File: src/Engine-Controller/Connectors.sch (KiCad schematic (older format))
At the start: 3 parts

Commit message: Annotated Schematic
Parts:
- removed None?: +VIN, symbol Engine-Controller:+VIN
- gave numbers to parts that had none: 2
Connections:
- net labels added: +VIN
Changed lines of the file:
@@
 $EndDescr
 $Comp
-L Engine-Controller:0901471110 J?
+L Engine-Controller:0901471110 J5
 U 1 1 60E3A3F9
 P 9150 1950
-F 0 "J?" H 9678 1553 60  0000 L CNN
+F 0 "J5" H 9678 1553 60  0000 L CNN
 F 1 "0901471110" H 9678 1447 60  0000 L CNN
 F 2 "66953-005LF_AMP" H 9300 750 60  0001 C CNN
@@
 	9050 4900 8800 4900
 $Comp
-L power:Earth #PWR?
+L power:Earth #PWR0112
 U 1 1 60DBDE57
 P 8800 5600
-F 0 "#PWR?" H 8800 5350 50  0001 C CNN
+F 0 "#PWR0112" H 8800 5350 50  0001 C CNN
 F 1 "Earth" H 8800 5450 50  0001 C CNN
 F 2 "" H 8800 5600 50  0001 C CNN
@@
 	9050 4400 8700 4400
 $Comp
-L Engine-Controller:+VIN None?
+L Engine-Controller:+VIN #None0101
 U 1 1 60E48282
 P 8700 4100
-F 0 "None?" H 8800 4100 50  0001 L CNN
+F 0 "#None0101" H 8800 4100 50  0001 L CNN
 F 1 "+VIN" H 8600 4200 50  0000 L CNN
 F 2 "" H 8700 4100 50  0001 C CNN
@@
 $EndComp
 $Comp
-L Engine-Controller:66953-005LF J?
+L Engine-Controller:66953-005LF J4
 U 1 1 60E41099
 P 9050 4400
-F 0 "J?" H 9578 4003 60  0000 L CNN
+F 0 "J4" H 9578 4003 60  0000 L CNN
 F 1 "66953-005LF" H 9578 3897 60  0000 L CNN
 F 2 "66953-005LF_AMP" H 9200 3200 60  0001 C CNN

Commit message: Associated Schematic Symbols with footprints
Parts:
- J5: footprint 66953-005LF_AMP -> Engine-Controller:0901471110
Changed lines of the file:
@@
 F 0 "J5" H 9678 1553 60  0000 L CNN
 F 1 "0901471110" H 9678 1447 60  0000 L CNN
-F 2 "66953-005LF_AMP" H 9300 750 60  0001 C CNN
+F 2 "Engine-Controller:0901471110" H 9300 750 60  0001 C CNN
 F 3 "" H 9150 1950 60  0000 C CNN
 	1    9150 1950

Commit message: Resolved all ERC issues
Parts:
- J4: footprint 66953-005LF_AMP -> Engine-Controller:66953-005LF
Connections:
- net labels removed: +VIN
- wire segments 23 -> 21
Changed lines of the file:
@@
 Comment4 ""
 $EndDescr
-$Comp
-L Engine-Controller:0901471110 J5
-U 1 1 60E3A3F9
-P 9150 1950
-F 0 "J5" H 9678 1553 60  0000 L CNN
-F 1 "0901471110" H 9678 1447 60  0000 L CNN
-F 2 "Engine-Controller:0901471110" H 9300 750 60  0001 C CNN
-F 3 "" H 9150 1950 60  0000 C CNN
-	1    9150 1950
-	1    0    0    -1
-$EndComp
 Text Notes 8300 1600 0    50   ~ 0
 IO Connector\n
@@
 	1    0    0    -1
 $EndComp
-Connection ~ 8700 4400
-Wire Wire Line
-	8550 4400 8700 4400
 Text GLabel 8550 4400 0    50   Input ~ 0
 VIN
-Wire Wire Line
-	8700 4400 8700 4250
-Wire Wire Line
-	9050 4400 8700 4400
-$Comp
-L Engine-Controller:+VIN #None0101
-U 1 1 60E48282
-P 8700 4100
-F 0 "#None0101" H 8800 4100 50  0001 L CNN
-F 1 "+VIN" H 8600 4200 50  0000 L CNN
-F 2 "" H 8700 4100 50  0001 C CNN
-F 3 "" H 8700 4100 50  0001 C CNN
-	1    8700 4100
-	1    0    0    -1
-$EndComp
-$Comp
-L Engine-Controller:66953-005LF J4
-U 1 1 60E41099
-P 9050 4400
-F 0 "J4" H 9578 4003 60  0000 L CNN
-F 1 "66953-005LF" H 9578 3897 60  0000 L CNN
-F 2 "66953-005LF_AMP" H 9200 3200 60  0001 C CNN
-F 3 "" H 9050 4400 60  0000 C CNN
-	1    9050 4400
-	1    0    0    -1
-$EndComp
 Wire Notes Line
 	10400 3900 10400 5800
@@
 Text GLabel 8100 2850 0    50   Input ~ 0
 IO10
-Wire Wire Line
-	9150 1950 8050 1950
-Wire Wire Line
-	9150 2050 8050 2050
-Wire Wire Line
-	9150 2150 8050 2150
-Wire Wire Line
-	9150 2250 8050 2250
-Wire Wire Line
-	9150 2350 8050 2350
-Wire Wire Line
-	9150 2450 8050 2450
-Wire Wire Line
-	9150 2550 8050 2550
-Wire Wire Line
-	9150 2650 8050 2650
-Wire Wire Line
-	9150 2750 8050 2750
-Wire Wire Line
-	9150 2850 8100 2850
 Wire Notes Line
 	7200 3200 7200 1700
@@
 Wire Notes Line
 	10450 3200 7200 3200
+$Comp
+L Engine-Controller:0901471110 J5
+U 1 1 6119F1F0
+P 9300 1950
+F 0 "J5" H 9828 1553 60  0000 L CNN
+F 1 "0901471110" H 9828 1447 60  0000 L CNN
+F 2 "Engine-Controller:0901471110" H 9450 750 60  0001 C CNN
+F 3 "" H 9300 1950 60  0000 C CNN
+	1    9300 1950
+	1    0    0    -1
+$EndComp
+Wire Wire Line
+	9300 1950 8050 1950
+Wire Wire Line
+	9300 2050 8050 2050
+Wire Wire Line
+	9300 2150 8050 2150
+Wire Wire Line
+	9300 2250 8050 2250
+Wire Wire Line
+	9300 2350 8050 2350
+Wire Wire Line
+	9300 2450 8050 2450
+Wire Wire Line
+	9300 2550 8050 2550
+Wire Wire Line
+	9300 2650 8050 2650
+Wire Wire Line
+	9300 2750 8050 2750
+Wire Wire Line
+	9300 2850 8100 2850
+$Comp
+L Engine-Controller:66953-005LF J4
+U 1 1 612955EA
+P 9050 4400
+F 0 "J4" H 9578 4003 60  0000 L CNN
+F 1 "66953-005LF" H 9578 3897 60  0000 L CNN
+F 2 "Engine-Controller:66953-005LF" H 9200 3200 60  0001 C CNN
+F 3 "" H 9050 4400 60  0000 C CNN
+	1    9050 4400
+	1    0    0    -1
+$EndComp
+Wire Wire Line
+	8550 4400 9050 4400
 $EndSCHEMATC

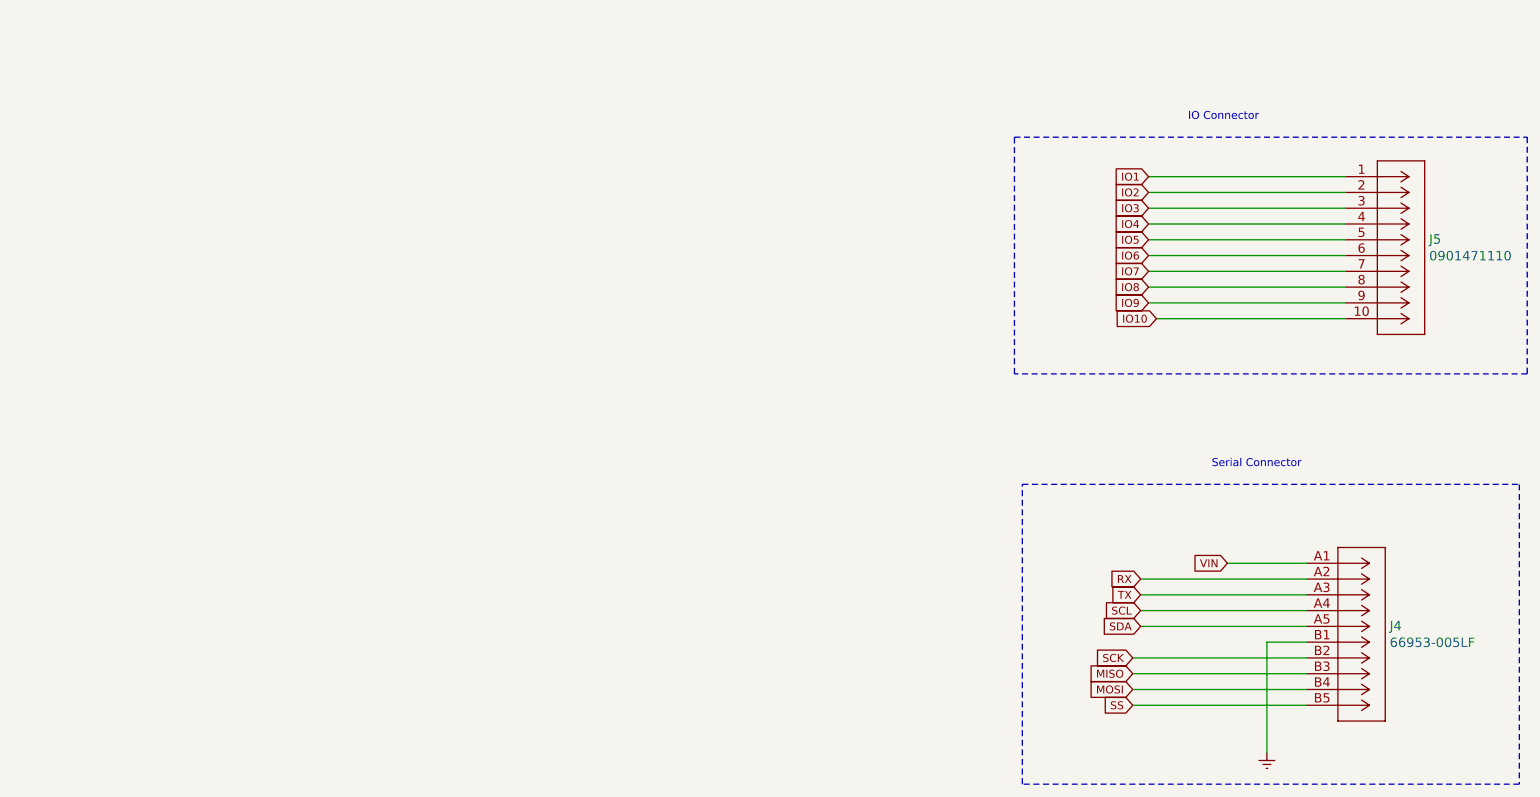
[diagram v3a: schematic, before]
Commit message: Added buffer to some IOs
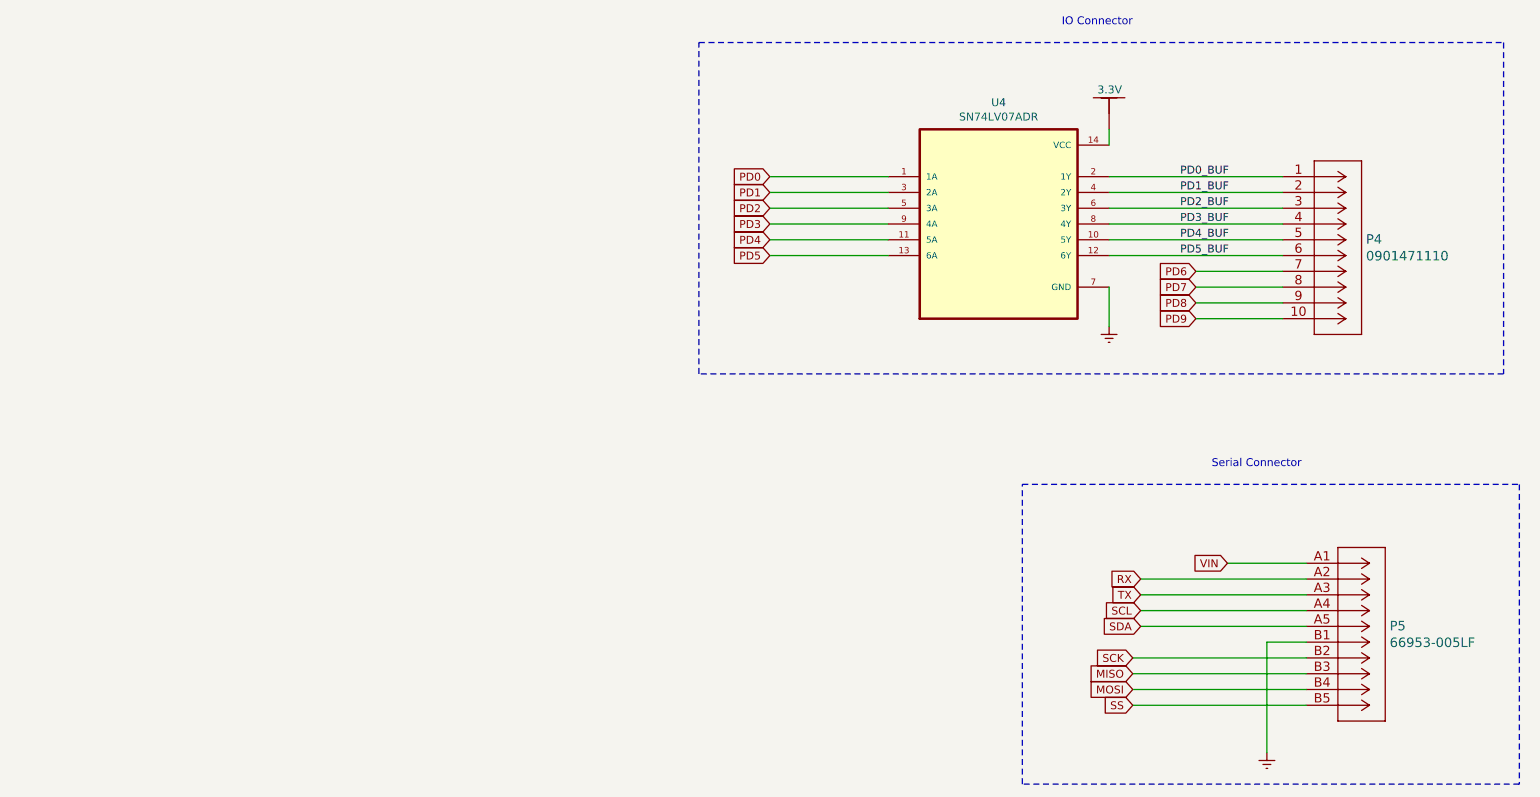
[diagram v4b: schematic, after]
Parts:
- removed J4: 66953-005LF, Engine-Controller:66953-005LF, symbol Engine-Controller:66953-005LF
- removed J5: 0901471110, Engine-Controller:0901471110, symbol Engine-Controller:0901471110
- added None02: 3.3V, symbol Engine-Controller:3.3V
- added P4: 0901471110, 66953-005LF_AMP, symbol Engine-Controller:0901471110
- added P5: 66953-005LF, 66953-005LF_AMP, symbol Engine-Controller:66953-005LF
- added U4: SN74LV07ADR, SOIC127P600X175-14N, symbol Engine-Controller:SN74LV07ADR
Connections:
- net Earth: now also P5.B1, U4.7 (GND)
- net MISO: now also P5.B3
- net MOSI: now also P5.B4
- net RX: now also P5.A2
- net SCK: now also P5.B2
- net SCL: now also P5.A4
- net SDA: now also P5.A5
- net SS: now also P5.B5
- net TX: now also P5.A3
- net VIN: now also P5.A1
- new net: None02.~, U4.14 (VCC)
- new net PD0: U4.1 (1A)
- new net PD0_BUF: P4.1, U4.2 (1Y)
- new net PD1: U4.3 (2A)
- new net PD1_BUF: P4.2, U4.4 (2Y)
- new net PD2: U4.5 (3A)
- new net PD2_BUF: P4.3, U4.6 (3Y)
- new net PD3: U4.9 (4A)
- new net PD3_BUF: P4.4, U4.8 (4Y)
- new net PD4: U4.11 (5A)
- new net PD4_BUF: P4.5, U4.10 (5Y)
- new net PD5: U4.13 (6A)
- new net PD5_BUF: P4.6, U4.12 (6Y)
- new net PD6: P4.7
- new net PD7: P4.8
- new net PD8: P4.9
- new net PD9: P4.10
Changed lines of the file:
@@
 Comment4 ""
 $EndDescr
-Text Notes 8300 1600 0    50   ~ 0
+Text Notes 7500 1000 0    50   ~ 0
 IO Connector\n
 Text Notes 8450 3800 0    50   ~ 0
@@
 Wire Notes Line
 	7250 3900 10400 3900
-Text GLabel 8050 1950 0    50   Input ~ 0
-IO1
-Text GLabel 8050 2050 0    50   Input ~ 0
-IO2
-Text GLabel 8050 2150 0    50   Input ~ 0
-IO3
-Text GLabel 8050 2250 0    50   Input ~ 0
-IO4
-Text GLabel 8050 2350 0    50   Input ~ 0
-IO5
-Text GLabel 8050 2450 0    50   Input ~ 0
-IO6
-Text GLabel 8050 2550 0    50   Input ~ 0
-IO7
-Text GLabel 8050 2650 0    50   Input ~ 0
-IO8
-Text GLabel 8050 2750 0    50   Input ~ 0
-IO9
-Text GLabel 8100 2850 0    50   Input ~ 0
-IO10
-Wire Notes Line
-	7200 3200 7200 1700
-Wire Notes Line
-	7200 1700 10450 1700
-Wire Notes Line
-	10450 1700 10450 3200
-Wire Notes Line
-	10450 3200 7200 3200
+Text GLabel 5650 1950 0    50   Input ~ 0
+PD0
+Text GLabel 5650 2050 0    50   Input ~ 0
+PD1
+Text GLabel 5650 2150 0    50   Input ~ 0
+PD2
+Text GLabel 5650 2250 0    50   Input ~ 0
+PD3
+Text GLabel 5650 2350 0    50   Input ~ 0
+PD4
+Text GLabel 5650 2450 0    50   Input ~ 0
+PD5
+Text GLabel 8350 2550 0    50   Input ~ 0
+PD6
+Text GLabel 8350 2650 0    50   Input ~ 0
+PD7
+Text GLabel 8350 2750 0    50   Input ~ 0
+PD8
+Text GLabel 8350 2850 0    50   Input ~ 0
+PD9
+Wire Wire Line
+	8550 4400 9050 4400
 $Comp
-L Engine-Controller:0901471110 J5
-U 1 1 6119F1F0
-P 9300 1950
-F 0 "J5" H 9828 1553 60  0000 L CNN
-F 1 "0901471110" H 9828 1447 60  0000 L CNN
-F 2 "Engine-Controller:0901471110" H 9450 750 60  0001 C CNN
-F 3 "" H 9300 1950 60  0000 C CNN
-	1    9300 1950
+L Engine-Controller:0901471110 P4
+U 1 1 61252CB3
+P 8900 1950
+F 0 "P4" H 9428 1553 60  0000 L CNN
+F 1 "0901471110" H 9428 1447 60  0000 L CNN
+F 2 "66953-005LF_AMP" H 9050 750 60  0001 C CNN
+F 3 "" H 8900 1950 60  0001 C CNN
+	1    8900 1950
 	1    0    0    -1
 $EndComp
-Wire Wire Line
-	9300 1950 8050 1950
-Wire Wire Line
-	9300 2050 8050 2050
-Wire Wire Line
-	9300 2150 8050 2150
-Wire Wire Line
-	9300 2250 8050 2250
-Wire Wire Line
-	9300 2350 8050 2350
-Wire Wire Line
-	9300 2450 8050 2450
-Wire Wire Line
-	9300 2550 8050 2550
-Wire Wire Line
-	9300 2650 8050 2650
-Wire Wire Line
-	9300 2750 8050 2750
-Wire Wire Line
-	9300 2850 8100 2850
 $Comp
-L Engine-Controller:66953-005LF J4
-U 1 1 612955EA
+L Engine-Controller:66953-005LF P5
+U 1 1 61255D75
 P 9050 4400
-F 0 "J4" H 9578 4003 60  0000 L CNN
+F 0 "P5" H 9578 4003 60  0000 L CNN
 F 1 "66953-005LF" H 9578 3897 60  0000 L CNN
-F 2 "Engine-Controller:66953-005LF" H 9200 3200 60  0001 C CNN
-F 3 "" H 9050 4400 60  0000 C CNN
+F 2 "66953-005LF_AMP" H 9200 3200 60  0001 C CNN
+F 3 "" H 9050 4400 60  0001 C CNN
 	1    9050 4400
 	1    0    0    -1
 $EndComp
 Wire Wire Line
-	8550 4400 9050 4400
+	5650 1950 6400 1950
+Wire Wire Line
+	5650 2050 6400 2050
+Wire Wire Line
+	5650 2150 6400 2150
+Wire Wire Line
+	5650 2250 6400 2250
+Wire Wire Line
+	5650 2350 6400 2350
+Wire Wire Line
+	5650 2450 6400 2450
+Wire Wire Line
+	7800 1950 8900 1950
+Wire Wire Line
+	7800 2050 8900 2050
+Wire Wire Line
+	7800 2150 8900 2150
+Wire Wire Line
+	7800 2250 8900 2250
+Wire Wire Line
+	7800 2350 8900 2350
+Wire Wire Line
+	7800 2450 8900 2450
+$Comp
+L power:Earth #PWR02
+U 1 1 6138D033
+P 7800 2900
+F 0 "#PWR02" H 7800 2650 50  0001 C CNN
+F 1 "Earth" H 7800 2750 50  0001 C CNN
+F 2 "" H 7800 2900 50  0001 C CNN
+F 3 "~" H 7800 2900 50  0001 C CNN
+	1    7800 2900
+	1    0    0    -1
+$EndComp
+Wire Wire Line
+	7800 2650 7800 2900
+$Comp
+L Engine-Controller:3.3V None02
+U 1 1 61392439
+P 7800 1500
+F 0 "None02" H 7928 1489 50  0001 L CNN
+F 1 "3.3V" H 7726 1601 50  0000 L CNN
+F 2 "" H 7800 1500 50  0001 C CNN
+F 3 "" H 7800 1500 50  0001 C CNN
+	1    7800 1500
+	1    0    0    -1
+$EndComp
+$Comp
+L Engine-Controller:SN74LV07ADR U4
+U 1 1 6134C986
+P 7100 2250
+F 0 "U4" H 7100 3020 50  0000 C CNN
+F 1 "SN74LV07ADR" H 7100 2929 50  0000 C CNN
+F 2 "SOIC127P600X175-14N" H 6650 1350 50  0001 L BNN
+F 3 "" H 7100 2250 50  0001 L BNN
+	1    7100 2250
+	1    0    0    -1
+$EndComp
+Wire Wire Line
+	7800 1750 7800 1650
+Wire Notes Line
+	5200 1100 10300 1100
+Wire Notes Line
+	10300 1100 10300 3200
+Wire Notes Line
+	10300 3200 5200 3200
+Wire Notes Line
+	5200 3200 5200 1100
+Text Label 8250 1950 0    50   ~ 0
+PD0_BUF
+Text Label 8250 2050 0    50   ~ 0
+PD1_BUF
+Text Label 8250 2250 0    50   ~ 0
+PD3_BUF
+Text Label 8250 2350 0    50   ~ 0
+PD4_BUF
+Text Label 8250 2150 0    50   ~ 0
+PD2_BUF
+Text Label 8250 2450 0    50   ~ 0
+PD5_BUF
+Wire Wire Line
+	8350 2550 8900 2550
+Wire Wire Line
+	8350 2650 8900 2650
+Wire Wire Line
+	8350 2750 8900 2750
+Wire Wire Line
+	8350 2850 8900 2850
 $EndSCHEMATC

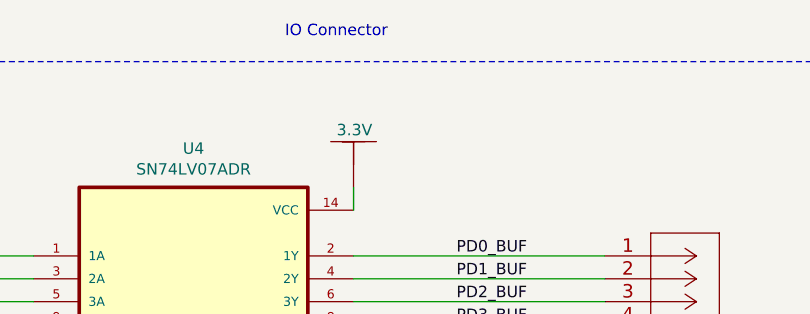
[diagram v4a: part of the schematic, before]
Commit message: Added NO Jumper to NRST button
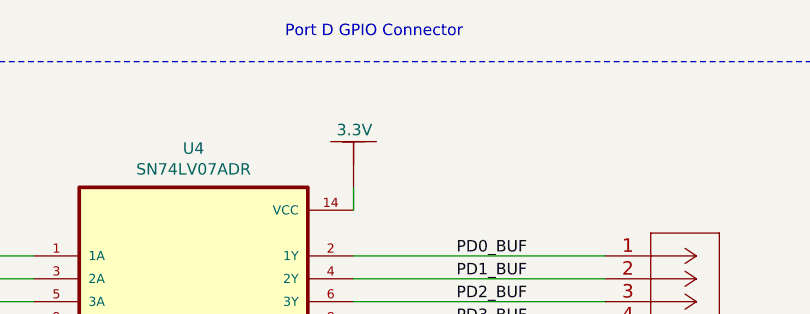
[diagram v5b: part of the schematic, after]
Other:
- note added: "Port D GPIO Connector\n"
- note removed: "IO Connector\n"
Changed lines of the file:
@@
 $EndDescr
 Text Notes 7500 1000 0    50   ~ 0
-IO Connector\n
+Port D GPIO Connector\n
 Text Notes 8450 3800 0    50   ~ 0
 Serial Connector

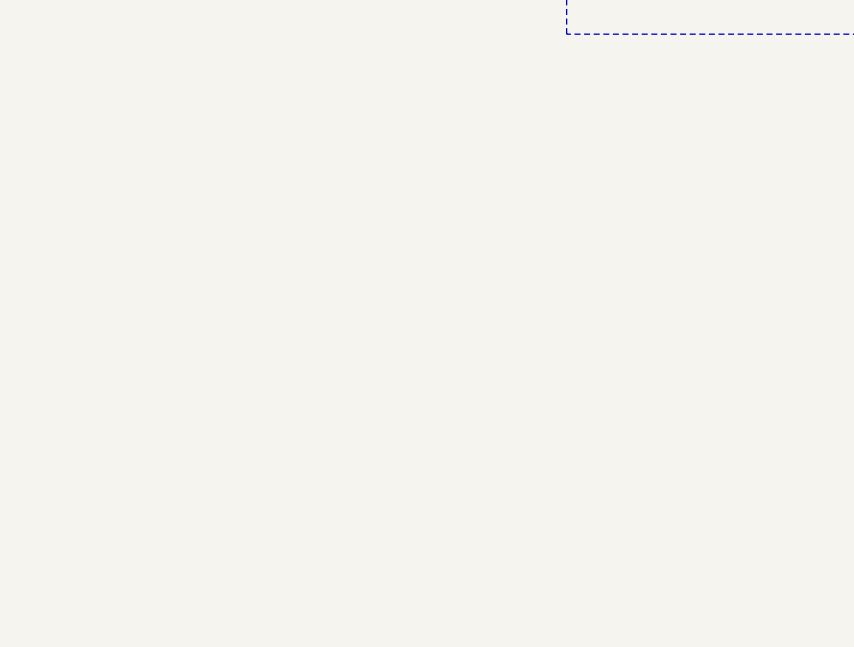
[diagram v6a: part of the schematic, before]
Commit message: Moved Programmer to connectors sheet
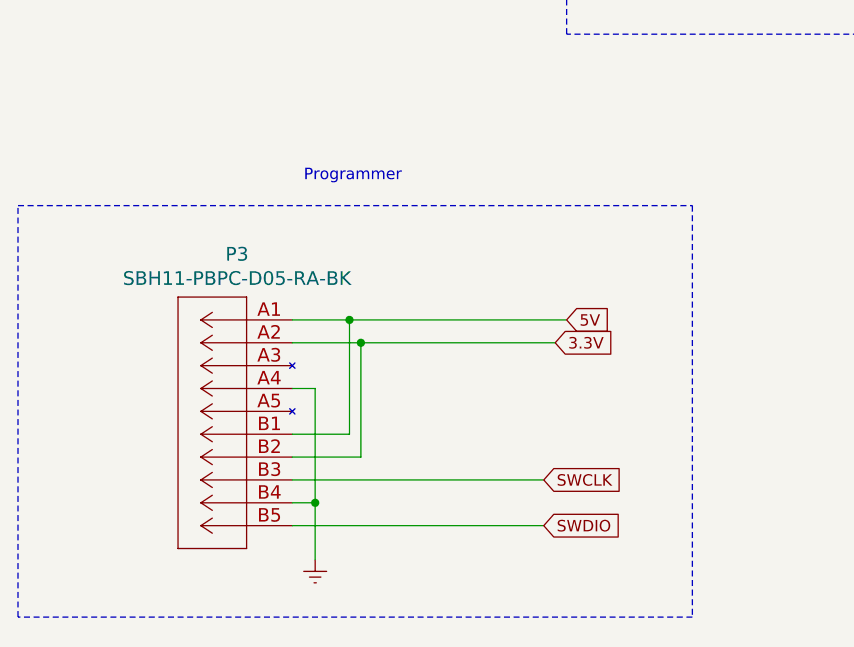
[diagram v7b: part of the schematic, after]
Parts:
- added P3: SBH11-PBPC-D05-RA-BK, 66953-005LF_AMP, symbol Engine-Controller:SBH11-PBPC-D05-RA-BK
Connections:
- net Earth: now also P3.A4, P3.B4
- new net 3.3V: P3.A2, P3.B2
- new net 5V: P3.A1, P3.B1
- new net SWCLK: P3.B3
- new net SWDIO: P3.B5
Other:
- note added: "Programmer\n"
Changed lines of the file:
@@
 $Descr A4 11693 8268
 encoding utf-8
-Sheet 5 6
+Sheet 4 5
 Title "Liquid Engine Microcontroller Connectors"
 Date "2021-06-29"
@@
 Wire Wire Line
 	8350 2850 8900 2850
+Text GLabel 5100 5150 2    50   Input ~ 0
+SWCLK
+Text GLabel 5100 5350 2    50   Input ~ 0
+SWDIO
+Text GLabel 5150 4550 2    50   Input ~ 0
+3.3V
+Text GLabel 5200 4450 2    50   Input ~ 0
+5V
+$Comp
+L power:Earth #PWR?
+U 1 1 6193D92B
+P 4100 5500
+AR Path="/60DAAA3E/6193D92B" Ref="#PWR?"  Part="1"
+AR Path="/60E24895/6193D92B" Ref="#PWR06"  Part="1"
+F 0 "#PWR06" H 4100 5250 50  0001 C CNN
+F 1 "Earth" H 4100 5350 50  0001 C CNN
+F 2 "" H 4100 5500 50  0001 C CNN
+F 3 "~" H 4100 5500 50  0001 C CNN
+	1    4100 5500
+	1    0    0    -1
+$EndComp
+$Comp
+L Engine-Controller:SBH11-PBPC-D05-RA-BK P?
+U 1 1 6193D931
+P 4000 4450
+AR Path="/60DAAA3E/6193D931" Ref="P?"  Part="1"
+AR Path="/60E24895/6193D931" Ref="P3"  Part="1"
+F 0 "P3" H 4242 4737 60  0000 C CNN
+F 1 "SBH11-PBPC-D05-RA-BK" H 4242 4631 60  0000 C CNN
+F 2 "66953-005LF_AMP" H 4150 3250 60  0001 C CNN
+F 3 "" H 4000 4450 60  0001 C CNN
+	1    4000 4450
+	-1   0    0    -1
+$EndComp
+Wire Wire Line
+	4000 4450 4250 4450
+Wire Wire Line
+	4000 4950 4250 4950
+Wire Wire Line
+	4250 4950 4250 4450
+Connection ~ 4250 4450
+Wire Wire Line
+	4250 4450 5200 4450
+Wire Wire Line
+	4000 4750 4100 4750
+Wire Wire Line
+	4100 4750 4100 5250
+Wire Wire Line
+	4000 5250 4100 5250
+Connection ~ 4100 5250
+Wire Wire Line
+	4100 5250 4100 5500
+Wire Wire Line
+	5150 4550 4300 4550
+Wire Wire Line
+	4000 5050 4300 5050
+Wire Wire Line
+	4300 5050 4300 4550
+Connection ~ 4300 4550
+Wire Wire Line
+	4300 4550 4000 4550
+Wire Wire Line
+	5100 5350 4000 5350
+Wire Wire Line
+	4000 5150 5100 5150
+Wire Notes Line
+	5750 3950 5750 5750
+Wire Notes Line
+	5750 5750 2800 5750
+Wire Notes Line
+	2800 5750 2800 3950
+Wire Notes Line
+	2800 3950 5750 3950
+Text Notes 4050 3850 0    50   ~ 0
+Programmer\n
 $EndSCHEMATC
